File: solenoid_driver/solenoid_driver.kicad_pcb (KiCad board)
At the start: 2 copper layers, 32.6 x 21.1 mm, 29 parts, among them J1 Conn_02x03_Odd_Even, J2 Conn_01x02, J3 Conn_01x02, J4 Conn_01x02, U1 FP6291, U2 ULN2003A, U3 TPS2553DBVR

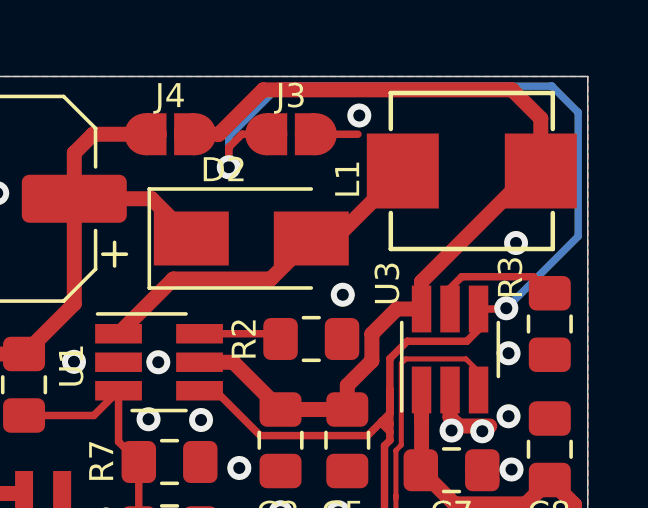
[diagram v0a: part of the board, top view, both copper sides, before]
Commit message: added version 1.0b with alternative inductor, because the inductor used by version 1.0 is low on stock. This variant has not been tested.
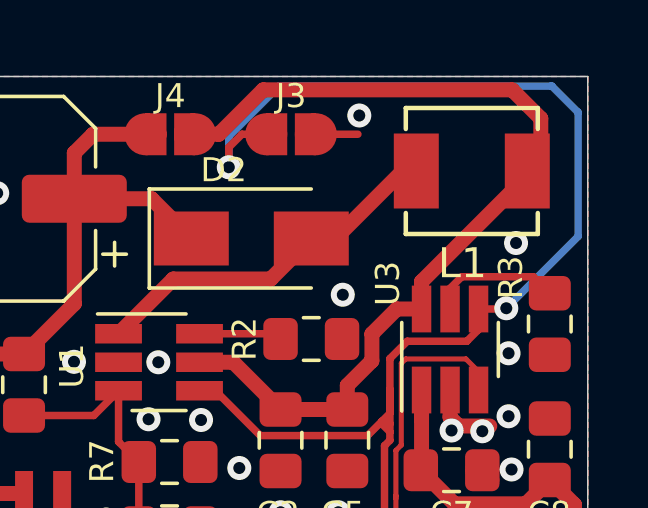
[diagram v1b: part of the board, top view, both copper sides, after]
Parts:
- L1: footprint solenoid_driver_footprint_library:footprint_for_MWSA0503_HANDSOLD -> solenoid_driver_footprint_library:footprint_for_MWSA0402
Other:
- board text added: "Solenoid Driver Rev 1.0b Designed by pandrew, based on original work by xwhatsit"
- board text removed: "Solenoid Driver Rev 1.0 Designed by pandrew, based on original work by xwhatsit"

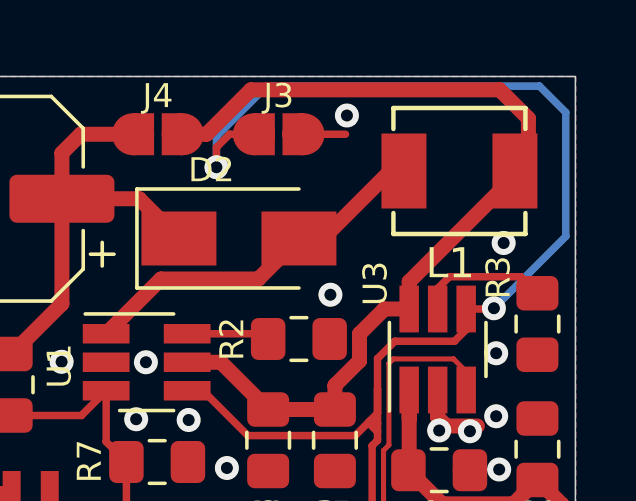
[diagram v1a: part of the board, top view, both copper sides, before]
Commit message: Use handsoldered footprint, add 3d model
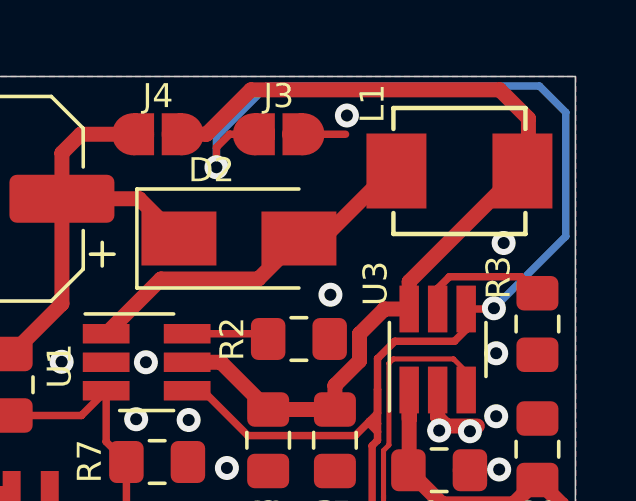
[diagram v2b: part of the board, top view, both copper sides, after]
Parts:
- L1: footprint solenoid_driver_footprint_library:footprint_for_MWSA0402 -> solenoid_driver_footprint_library:footprint_for_MWSA0402_HANDSOLD
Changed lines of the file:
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@@
     (add_net TRIGGER)
   )
-  (module solenoid_driver_footprint_library:footprint_for_MWSA0402 (layer F.Cu)
+  (module solenoid_driver_footprint_library:footprint_for_MWSA0402_HANDSOLD (layer F.Cu)
     (at 130.45 91.35 180)
     (attr smd)
-    (fp_text reference L1 (at 0.30922 -3.07778) (layer F.SilkS)
-      (effects (font (size 1 1) (thickness 0.15)))
+    (fp_text reference L1 (at 2.9 2.25 90) (layer F.SilkS)
+      (effects (font (size 0.8 0.8) (thickness 0.15)))
     )
     (fp_text value 4.7uH (at 0.30922 -4.07778) (layer F.Fab)
       (effects (font (size 1 1) (thickness 0.15)))
     )
+    (fp_line (start 2.4 -2.3) (end 2.4 2.3) (layer F.CrtYd) (width 0.12))
+    (fp_line (start -2.2 2.1) (end -2.2 1.4) (layer F.SilkS) (width 0.15))
+    (fp_line (start -2.2 -2.1) (end -2.2 -1.4) (layer F.SilkS) (width 0.15))
+    (fp_line (start 2.2 2.1) (end 2.2 1.4) (layer F.SilkS) (width 0.15))
+    (fp_line (start 2.2 -2.1) (end 2.2 -1.4) (layer F.SilkS) (width 0.15))
+    (fp_line (start -2.4 2.3) (end -2.4 -2.3) (layer F.CrtYd) (width 0.12))
+    (fp_line (start 2.4 2.3) (end -2.4 2.3) (layer F.CrtYd) (width 0.12))
+    (fp_line (start -2.4 -2.3) (end 2.4 -2.3) (layer F.CrtYd) (width 0.12))
     (fp_line (start 2.2 -2.1) (end -2.2 -2.1) (layer F.SilkS) (width 0.15))
     (fp_line (start -2.2 2.1) (end 2.2 2.1) (layer F.SilkS) (width 0.15))
-    (fp_line (start -2.2 -2.1) (end -2.2 -1.4) (layer F.SilkS) (width 0.15))
-    (fp_line (start -2.2 2.1) (end -2.2 1.4) (layer F.SilkS) (width 0.15))
-    (fp_line (start 2.2 2.1) (end 2.2 1.4) (layer F.SilkS) (width 0.15))
-    (fp_line (start 2.2 -2.1) (end 2.2 -1.4) (layer F.SilkS) (width 0.15))
-    (fp_line (start -2.4 -2.3) (end 2.4 -2.3) (layer F.CrtYd) (width 0.12))
-    (fp_line (start 2.4 -2.3) (end 2.4 2.3) (layer F.CrtYd) (width 0.12))
-    (fp_line (start 2.4 2.3) (end -2.4 2.3) (layer F.CrtYd) (width 0.12))
-    (fp_line (start -2.4 2.3) (end -2.4 -2.3) (layer F.CrtYd) (width 0.12))
-    (pad 2 smd rect (at 1.85 0 180) (size 1.5 2.5) (layers F.Cu F.Paste F.Mask)
+    (pad 2 smd rect (at 2.1 0 180) (size 2 2.5) (layers F.Cu F.Paste F.Mask)
       (net 9 SWITCHING_NODE))
-    (pad 1 smd rect (at -1.85 0 180) (size 1.5 2.5) (layers F.Cu F.Paste F.Mask)
+    (pad 1 smd rect (at -2.1 0 180) (size 2 2.5) (layers F.Cu F.Paste F.Mask)
       (net 13 LIMITED5V))
+    (model inductor_mwsa0402.step
+      (at (xyz 0 0 0))
+      (scale (xyz 1 1 1))
+      (rotate (xyz 0 0 0))
+    )
   )
   (module solenoid_driver_footprint_library:tooling_hole (layer F.Cu)
